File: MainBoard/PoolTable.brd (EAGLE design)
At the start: 457.2 x 166 mm, 75 parts, among them IC1 LM317MBSTT3, IC2 LM317MBSTT3, IC3 LM317MBSTT3, IC5 MIC2026-1YM, IC7 AP2331W-7, J1 USB_A_SMT_FEMALE, J2 USB_A_SMT_FEMALE, J4 SD_CARD_SOCKET, Q1 DMG1012T-7, Q2 DMG1012T-7, Q3 DMG1012T-7, U1 TMP102, U2 TMP102, U3 TMP102, U4 TMP102, U5 LAN9512-JZX, U6 FSUSB42UMX

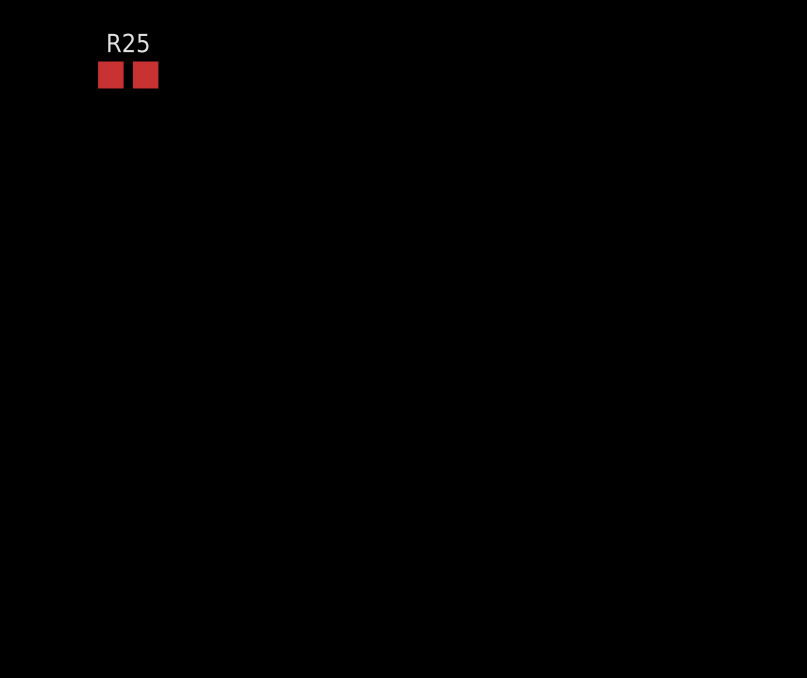
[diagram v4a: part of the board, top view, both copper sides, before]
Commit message: Implementing Cameras
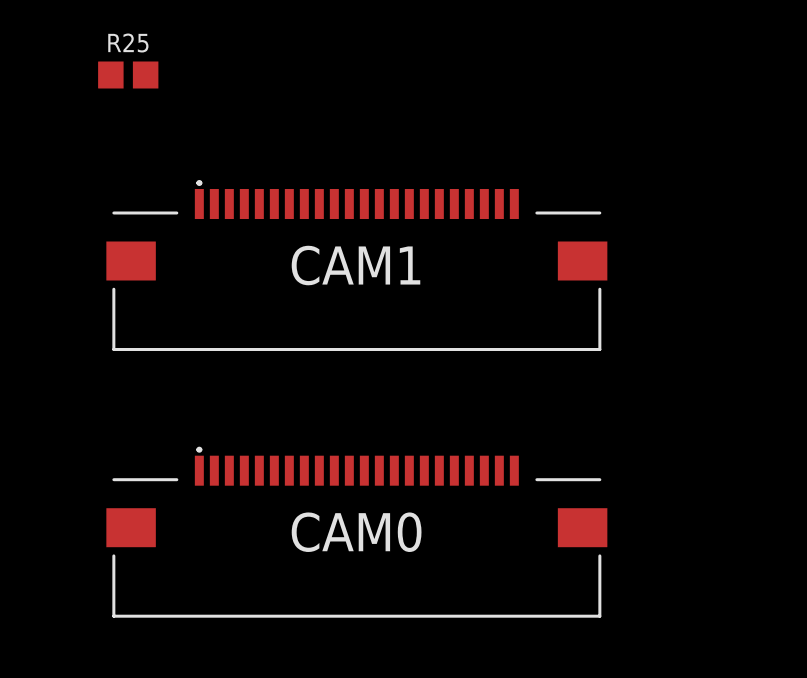
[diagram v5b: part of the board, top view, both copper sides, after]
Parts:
- added CAM0, CAM1: 54548-2271, SamacSys_Parts:545482271
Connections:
- new net CPU1_CAM0_C_N: CAM0.8
- new net CPU1_CAM0_C_P: CAM0.9
- new net CPU1_CAM0_D0_N: CAM0.2
- new net CPU1_CAM0_D0_P: CAM0.3
- new net CPU1_CAM0_D1_N: CAM0.5
- new net CPU1_CAM0_D1_P: CAM0.6
- new net CPU1_CAM0_IO_0: CAM0.17
- new net CPU1_CAM0_IO_1: CAM0.18
- new net CPU1_CAM1_C_N: CAM1.8, CPU1.149
- new net CPU1_CAM1_C_P: CAM1.9, CPU1.147
- new net CPU1_CAM1_D0_N: CAM1.2, CPU1.161
- new net CPU1_CAM1_D0_P: CAM1.3, CPU1.159
- new net CPU1_CAM1_D1_N: CAM1.5, CPU1.155
- new net CPU1_CAM1_D1_P: CAM1.6, CPU1.153
- new net CPU1_CAM1_D2_N: CAM1.11, CPU1.143
- new net CPU1_CAM1_D2_P: CAM1.12, CPU1.141
- new net CPU1_CAM1_D3_N: CAM1.14, CPU1.137
- new net CPU1_CAM1_D3_P: CAM1.15, CPU1.135
- new net CPU1_CAM1_IO_0: CAM1.17
- new net CPU1_CAM1_IO_1: CAM1.18
- new net CPU1_CD1_SCL: CAM0.20, CAM1.20
- new net CPU1_CD1_SDA: CAM0.21, CAM1.21
- net 3.3V: now also CAM0.22, CAM1.22
- net GND: now also CAM0.1, CAM0.10, CAM0.13, CAM0.16, CAM0.19, CAM0.23, CAM0.24, CAM0.4, CAM0.7, CAM1.1, CAM1.10, CAM1.13, CAM1.16, CAM1.19, CAM1.23, CAM1.24, CAM1.4, CAM1.7
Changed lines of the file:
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@@
 <attribute name="VALUE" x="-59.69" y="-436.372" size="0.6096" layer="27" font="vector" ratio="20" align="top-center"/>
+</element>
+<element name="CAM1" library="SamacSys_Parts" package="545482271" value="54548-2271" x="-52.07" y="-441.96" smashed="yes">
+<attribute name="DESCRIPTION" value="FFC &amp; FPC Connectors 0.5 FPC ZIF Hsg Assy ssy 22Ckt EmbsTp Pkg" x="-52.07" y="-441.96" size="1.778" layer="27" display="off"/>
+<attribute name="HEIGHT" value="1mm" x="-52.07" y="-441.96" size="1.778" layer="27" display="off"/>
+<attribute name="MANUFACTURER_NAME" value="Molex" x="-52.07" y="-441.96" size="1.778" layer="27" display="off"/>
+<attribute name="MANUFACTURER_PART_NUMBER" value="54548-2271" x="-52.07" y="-441.96" size="1.778" layer="27" display="off"/>
+<attribute name="MOUSER_PART_NUMBER" value="538-54548-2271" x="-52.07" y="-441.96" size="1.778" layer="27" display="off"/>
+<attribute name="NAME" x="-52.07" y="-441.96" size="1.27" layer="25" align="center"/>
+<attribute name="VALUE" x="-52.07" y="-441.96" size="1.27" layer="27" align="center"/>
+</element>
+<element name="CAM0" library="SamacSys_Parts" package="545482271" value="54548-2271" x="-52.07" y="-450.85" smashed="yes">
+<attribute name="DESCRIPTION" value="FFC &amp; FPC Connectors 0.5 FPC ZIF Hsg Assy ssy 22Ckt EmbsTp Pkg" x="-52.07" y="-450.85" size="1.778" layer="27" display="off"/>
+<attribute name="HEIGHT" value="1mm" x="-52.07" y="-450.85" size="1.778" layer="27" display="off"/>
+<attribute name="MANUFACTURER_NAME" value="Molex" x="-52.07" y="-450.85" size="1.778" layer="27" display="off"/>
+<attribute name="MANUFACTURER_PART_NUMBER" value="54548-2271" x="-52.07" y="-450.85" size="1.778" layer="27" display="off"/>
+<attribute name="MOUSER_PART_NUMBER" value="538-54548-2271" x="-52.07" y="-450.85" size="1.778" layer="27" display="off"/>
+<attribute name="NAME" x="-52.07" y="-450.85" size="1.27" layer="25" align="center"/>
+<attribute name="VALUE" x="-52.07" y="-450.85" size="1.27" layer="27" align="center"/>
 </element>
 </elements>
@@
 <contactref element="U$4" pad="2"/>
 <contactref element="U$5" pad="2"/>
+<contactref element="CAM1" pad="1"/>
+<contactref element="CAM1" pad="4"/>
+<contactref element="CAM1" pad="7"/>
+<contactref element="CAM1" pad="10"/>
+<contactref element="CAM1" pad="13"/>
+<contactref element="CAM1" pad="16"/>
+<contactref element="CAM1" pad="19"/>
+<contactref element="CAM1" pad="23"/>
+<contactref element="CAM1" pad="24"/>
+<contactref element="CAM0" pad="1"/>
+<contactref element="CAM0" pad="4"/>
+<contactref element="CAM0" pad="7"/>
+<contactref element="CAM0" pad="10"/>
+<contactref element="CAM0" pad="13"/>
+<contactref element="CAM0" pad="16"/>
+<contactref element="CAM0" pad="19"/>
+<contactref element="CAM0" pad="23"/>
+<contactref element="CAM0" pad="24"/>
+<wire x1="-55.82" y1="-448.8" x2="-57.32" y2="-448.8" width="0" layer="19" extent="1-1"/>
+<wire x1="-54.32" y1="-448.8" x2="-55.82" y2="-448.8" width="0" layer="19" extent="1-1"/>
+<wire x1="-52.82" y1="-448.8" x2="-54.32" y2="-448.8" width="0" layer="19" extent="1-1"/>
+<wire x1="-51.32" y1="-448.8" x2="-52.82" y2="-448.8" width="0" layer="19" extent="1-1"/>
+<wire x1="-49.82" y1="-448.8" x2="-51.32" y2="-448.8" width="0" layer="19" extent="1-1"/>
+<wire x1="-48.32" y1="-448.8" x2="-49.82" y2="-448.8" width="0" layer="19" extent="1-1"/>
+<wire x1="-59.595" y1="-450.7" x2="-57.32" y2="-448.8" width="0" layer="19" extent="1-1"/>
+<wire x1="-44.545" y1="-450.7" x2="-48.32" y2="-448.8" width="0" layer="19" extent="1-1"/>
+<wire x1="-59.595" y1="-441.81" x2="-57.32" y2="-448.8" width="0" layer="19" extent="1-1"/>
+<wire x1="-57.32" y1="-439.91" x2="-59.595" y2="-441.81" width="0" layer="19" extent="1-1"/>
+<wire x1="-55.82" y1="-439.91" x2="-57.32" y2="-439.91" width="0" layer="19" extent="1-1"/>
+<wire x1="-54.32" y1="-439.91" x2="-55.82" y2="-439.91" width="0" layer="19" extent="1-1"/>
+<wire x1="-52.82" y1="-439.91" x2="-54.32" y2="-439.91" width="0" layer="19" extent="1-1"/>
+<wire x1="-51.32" y1="-439.91" x2="-52.82" y2="-439.91" width="0" layer="19" extent="1-1"/>
+<wire x1="-49.82" y1="-439.91" x2="-51.32" y2="-439.91" width="0" layer="19" extent="1-1"/>
+<wire x1="-48.32" y1="-439.91" x2="-49.82" y2="-439.91" width="0" layer="19" extent="1-1"/>
+<wire x1="-44.545" y1="-441.81" x2="-48.32" y2="-439.91" width="0" layer="19" extent="1-1"/>
+<wire x1="-59.11" y1="-435.61" x2="-57.32" y2="-439.91" width="0" layer="19" extent="1-1"/>
 <wire x1="-59.11" y1="-431.8" x2="-59.11" y2="-435.61" width="0" layer="19" extent="1-1"/>
 <wire x1="-59.11" y1="-427.99" x2="-59.11" y2="-431.8" width="0" layer="19" extent="1-1"/>
@@
 <contactref element="C12" pad="1"/>
 <contactref element="SJ1" pad="2"/>
+<contactref element="CAM1" pad="22"/>
+<contactref element="CAM0" pad="22"/>
+<wire x1="-46.82" y1="-439.91" x2="-46.82" y2="-448.8" width="0" layer="19" extent="1-1"/>
+<wire x1="-58.928" y1="-416.56" x2="-46.82" y2="-439.91" width="0" layer="19" extent="1-1"/>
 <wire x1="-60.54" y1="-411.48" x2="-58.928" y2="-416.56" width="0" layer="19" extent="1-1"/>
 <wire x1="-60.69" y1="-395.7" x2="-60.54" y2="-411.48" width="0" layer="19" extent="1-1"/>
@@
 <contactref element="U5" pad="3"/>
 </signal>
+<signal name="CPU1_CAM1_D3_P" class="1">
+<contactref element="CPU1" pad="135"/>
+<contactref element="CAM1" pad="15"/>
+<wire x1="38.39" y1="55.6" x2="-50.32" y2="-439.91" width="0" layer="19" extent="1-1"/>
+</signal>
+<signal name="CPU1_CAM1_D3_N" class="1">
+<contactref element="CPU1" pad="137"/>
+<contactref element="CAM1" pad="14"/>
+<wire x1="38.39" y1="56.2" x2="-50.82" y2="-439.91" width="0" layer="19" extent="1-1"/>
+</signal>
+<signal name="CPU1_CAM1_D2_P" class="1">
+<contactref element="CPU1" pad="141"/>
+<contactref element="CAM1" pad="12"/>
+<wire x1="38.39" y1="57.4" x2="-51.82" y2="-439.91" width="0" layer="19" extent="1-1"/>
+</signal>
+<signal name="CPU1_CAM1_D2_N" class="1">
+<contactref element="CPU1" pad="143"/>
+<contactref element="CAM1" pad="11"/>
+<wire x1="38.39" y1="58" x2="-52.32" y2="-439.91" width="0" layer="19" extent="1-1"/>
+</signal>
+<signal name="CPU1_CAM1_C_P" class="1">
+<contactref element="CPU1" pad="147"/>
+<contactref element="CAM1" pad="9"/>
+<wire x1="38.39" y1="59.2" x2="-53.32" y2="-439.91" width="0" layer="19" extent="1-1"/>
+</signal>
+<signal name="CPU1_CAM1_C_N" class="1">
+<contactref element="CPU1" pad="149"/>
+<contactref element="CAM1" pad="8"/>
+<wire x1="38.39" y1="59.8" x2="-53.82" y2="-439.91" width="0" layer="19" extent="1-1"/>
+</signal>
+<signal name="CPU1_CAM1_D1_P" class="1">
+<contactref element="CPU1" pad="153"/>
+<contactref element="CAM1" pad="6"/>
+<wire x1="38.39" y1="61" x2="-54.82" y2="-439.91" width="0" layer="19" extent="1-1"/>
+</signal>
+<signal name="CPU1_CAM1_D1_N" class="1">
+<contactref element="CPU1" pad="155"/>
+<contactref element="CAM1" pad="5"/>
+<wire x1="38.39" y1="61.6" x2="-55.32" y2="-439.91" width="0" layer="19" extent="1-1"/>
+</signal>
+<signal name="CPU1_CAM1_D0_P" class="1">
+<contactref element="CPU1" pad="159"/>
+<contactref element="CAM1" pad="3"/>
+<wire x1="38.39" y1="62.8" x2="-56.32" y2="-439.91" width="0" layer="19" extent="1-1"/>
+</signal>
+<signal name="CPU1_CAM1_D0_N" class="1">
+<contactref element="CPU1" pad="161"/>
+<contactref element="CAM1" pad="2"/>
+<wire x1="38.39" y1="63.4" x2="-56.82" y2="-439.91" width="0" layer="19" extent="1-1"/>
+</signal>
+<signal name="CPU1_CAM1_IO_0">
+<contactref element="CAM1" pad="17"/>
+</signal>
+<signal name="CPU1_CAM1_IO_1">
+<contactref element="CAM1" pad="18"/>
+</signal>
+<signal name="CPU1_CD1_SCL">
+<contactref element="CAM1" pad="20"/>
+<contactref element="CAM0" pad="20"/>
+<wire x1="-47.82" y1="-439.91" x2="-47.82" y2="-448.8" width="0" layer="19" extent="1-1"/>
+</signal>
+<signal name="CPU1_CD1_SDA">
+<contactref element="CAM1" pad="21"/>
+<contactref element="CAM0" pad="21"/>
+<wire x1="-47.32" y1="-439.91" x2="-47.32" y2="-448.8" width="0" layer="19" extent="1-1"/>
+</signal>
+<signal name="CPU1_CAM0_D0_N">
+<contactref element="CAM0" pad="2"/>
+</signal>
+<signal name="CPU1_CAM0_D0_P">
+<contactref element="CAM0" pad="3"/>
+</signal>
+<signal name="CPU1_CAM0_D1_N">
+<contactref element="CAM0" pad="5"/>
+</signal>
+<signal name="CPU1_CAM0_D1_P">
+<contactref element="CAM0" pad="6"/>
+</signal>
+<signal name="CPU1_CAM0_C_N">
+<contactref element="CAM0" pad="8"/>
+</signal>
+<signal name="CPU1_CAM0_C_P">
+<contactref element="CAM0" pad="9"/>
+</signal>
+<signal name="CPU1_CAM0_IO_0">
+<contactref element="CAM0" pad="17"/>
+</signal>
+<signal name="CPU1_CAM0_IO_1">
+<contactref element="CAM0" pad="18"/>
+</signal>
 </signals>

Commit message: Syncing work
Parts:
- added SJ2, SJ3, SJ4, SJ5, SJ6, SJ7, SJ8, SJ9: (no value), jumper:SJ
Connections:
- removed net CPU1_CD1_SCL: CAM0.20, CAM1.20
- removed net CPU1_CD1_SDA: CAM0.21, CAM1.21
- new net CPU1_CAM0_IO0: SJ9.1
- new net CPU1_CAM0_IO1: SJ8.1
- new net CPU1_CAM0_SCL: SJ7.1
- new net CPU1_CAM0_SDA: SJ6.1
- new net CPU1_CAM1_IO0: SJ5.1
- new net CPU1_CAM1_IO1: SJ4.1
- new net CPU1_CAM1_SCL: SJ3.1
- new net CPU1_CAM1_SDA: SJ2.1
- net CPU1_CAM0_C_N: now also CPU1.144
- net CPU1_CAM0_C_P: now also CPU1.142
- net CPU1_CAM0_D0_N: now also CPU1.138
- net CPU1_CAM0_D0_P: now also CPU1.136
- net CPU1_CAM0_D1_N: now also CPU1.150
- net CPU1_CAM0_D1_P: now also CPU1.148
- net CPU1_GPIO28: now also SJ6.2
- net CPU1_GPIO29: now also SJ7.2
- net CPU1_GPIO30: now also SJ8.2
- net CPU1_GPIO31: now also SJ9.2
- net CPU1_SCL0: now also SJ3.2
- net CPU1_SCL1: now also SJ5.2
- net CPU1_SDA0: now also SJ2.2
- net CPU1_SDA1: now also SJ4.2
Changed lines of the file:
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@@
 <attribute name="VALUE" x="-52.07" y="-450.85" size="1.27" layer="27" align="center"/>
+</element>
+<element name="SJ2" library="jumper" library_urn="urn:adsk.eagle:library:252" package="SJ" package3d_urn="urn:adsk.eagle:package:15471/1" value="" x="-59.69" y="-458.47" smashed="yes">
+<attribute name="NAME" x="-61.341" y="-457.327" size="1.27" layer="25" ratio="10"/>
+<attribute name="VALUE" x="-59.2899" y="-458.47" size="0.02" layer="27"/>
+</element>
+<element name="SJ3" library="jumper" library_urn="urn:adsk.eagle:library:252" package="SJ" package3d_urn="urn:adsk.eagle:package:15471/1" value="" x="-59.69" y="-463.55" smashed="yes">
+<attribute name="NAME" x="-61.341" y="-462.407" size="1.27" layer="25" ratio="10"/>
+<attribute name="VALUE" x="-59.2899" y="-463.55" size="0.02" layer="27"/>
+</element>
+<element name="SJ4" library="jumper" library_urn="urn:adsk.eagle:library:252" package="SJ" package3d_urn="urn:adsk.eagle:package:15471/1" value="" x="-59.69" y="-468.63" smashed="yes">
+<attribute name="NAME" x="-61.341" y="-467.487" size="1.27" layer="25" ratio="10"/>
+<attribute name="VALUE" x="-59.2899" y="-468.63" size="0.02" layer="27"/>
+</element>
+<element name="SJ5" library="jumper" library_urn="urn:adsk.eagle:library:252" package="SJ" package3d_urn="urn:adsk.eagle:package:15471/1" value="" x="-59.69" y="-473.71" smashed="yes">
+<attribute name="NAME" x="-61.341" y="-472.567" size="1.27" layer="25" ratio="10"/>
+<attribute name="VALUE" x="-59.2899" y="-473.71" size="0.02" layer="27"/>
+</element>
+<element name="SJ6" library="jumper" library_urn="urn:adsk.eagle:library:252" package="SJ" package3d_urn="urn:adsk.eagle:package:15471/1" value="" x="-59.69" y="-478.79" smashed="yes">
+<attribute name="NAME" x="-61.341" y="-477.647" size="1.27" layer="25" ratio="10"/>
+<attribute name="VALUE" x="-59.2899" y="-478.79" size="0.02" layer="27"/>
+</element>
+<element name="SJ7" library="jumper" library_urn="urn:adsk.eagle:library:252" package="SJ" package3d_urn="urn:adsk.eagle:package:15471/1" value="" x="-59.69" y="-483.87" smashed="yes">
+<attribute name="NAME" x="-61.341" y="-482.727" size="1.27" layer="25" ratio="10"/>
+<attribute name="VALUE" x="-59.2899" y="-483.87" size="0.02" layer="27"/>
+</element>
+<element name="SJ8" library="jumper" library_urn="urn:adsk.eagle:library:252" package="SJ" package3d_urn="urn:adsk.eagle:package:15471/1" value="" x="-59.69" y="-488.95" smashed="yes">
+<attribute name="NAME" x="-61.341" y="-487.807" size="1.27" layer="25" ratio="10"/>
+<attribute name="VALUE" x="-59.2899" y="-488.95" size="0.02" layer="27"/>
+</element>
+<element name="SJ9" library="jumper" library_urn="urn:adsk.eagle:library:252" package="SJ" package3d_urn="urn:adsk.eagle:package:15471/1" value="" x="-59.69" y="-494.03" smashed="yes">
+<attribute name="NAME" x="-61.341" y="-492.887" size="1.27" layer="25" ratio="10"/>
+<attribute name="VALUE" x="-59.2899" y="-494.03" size="0.02" layer="27"/>
 </element>
 </elements>
@@
 <contactref element="U$3" pad="SDA"/>
 <contactref element="U$2" pad="SDA"/>
+<contactref element="SJ2" pad="2"/>
 <wire x1="19.05" y1="-212.09" x2="19.05" y2="-242.57" width="0" layer="19" extent="1-1"/>
 <wire x1="19.05" y1="-181.61" x2="19.05" y2="-212.09" width="0" layer="19" extent="1-1"/>
@@
 <wire x1="-1.763584375" y1="-121.42203125" x2="-5.573584375" y2="-121.42203125" width="0" layer="19" extent="1-1"/>
 <wire x1="38.39" y1="12.4" x2="-1.763584375" y2="-121.42203125" width="0" layer="19" extent="1-1"/>
+<wire x1="-58.928" y1="-458.47" x2="19.05" y2="-242.57" width="0" layer="19" extent="1-1"/>
 </signal>
 <signal name="CPU1_SCL0">
@@
 <contactref element="U$3" pad="SCL"/>
 <contactref element="U$2" pad="SCL"/>
+<contactref element="SJ3" pad="2"/>
 <wire x1="19.05" y1="-214.63" x2="19.05" y2="-245.11" width="0" layer="19" extent="1-1"/>
 <wire x1="19.05" y1="-184.15" x2="19.05" y2="-214.63" width="0" layer="19" extent="1-1"/>
@@
 <wire x1="-3.34" y1="-121.42203125" x2="-7.15" y2="-121.42203125" width="0" layer="19" extent="1-1"/>
 <wire x1="38.39" y1="13" x2="-3.34" y2="-121.42203125" width="0" layer="19" extent="1-1"/>
+<wire x1="-58.928" y1="-463.55" x2="19.05" y2="-245.11" width="0" layer="19" extent="1-1"/>
 </signal>
 <signal name="CPU1_SDA1">
 <contactref element="CPU1" pad="9"/>
 <contactref element="R11" pad="1"/>
+<contactref element="SJ4" pad="2"/>
 <wire x1="38.39" y1="14.2" x2="-11.01" y2="-175.26" width="0" layer="19" extent="1-1"/>
+<wire x1="-58.928" y1="-468.63" x2="-11.01" y2="-175.26" width="0" layer="19" extent="1-1"/>
 </signal>
 <signal name="CPU1_SCL1">
 <contactref element="CPU1" pad="11"/>
 <contactref element="R10" pad="1"/>
+<contactref element="SJ5" pad="2"/>
 <wire x1="38.39" y1="14.8" x2="-11.01" y2="-171.45" width="0" layer="19" extent="1-1"/>
+<wire x1="-58.928" y1="-473.71" x2="-11.01" y2="-171.45" width="0" layer="19" extent="1-1"/>
 </signal>
 <signal name="CPU1_GPIO4">
@@
 <contactref element="CPU1" pad="28"/>
 <contactref element="R22" pad="1"/>
+<contactref element="SJ6" pad="2"/>
+<wire x1="-58.928" y1="-478.79" x2="-60.27" y2="-424.18" width="0" layer="19" extent="1-1"/>
 <wire x1="30.19" y1="19.9" x2="-60.27" y2="-424.18" width="0" layer="19" extent="1-1"/>
 </signal>
@@
 <contactref element="CPU1" pad="30"/>
 <contactref element="R23" pad="1"/>
+<contactref element="SJ7" pad="2"/>
+<wire x1="-58.928" y1="-483.87" x2="-60.27" y2="-427.99" width="0" layer="19" extent="1-1"/>
 <wire x1="30.19" y1="20.5" x2="-60.27" y2="-427.99" width="0" layer="19" extent="1-1"/>
 </signal>
 <signal name="CPU1_GPIO30">
 <contactref element="CPU1" pad="34"/>
+<contactref element="SJ8" pad="2"/>
+<wire x1="-58.928" y1="-488.95" x2="30.19" y2="21.7" width="0" layer="19" extent="1-1"/>
 </signal>
 <signal name="CPU1_GPIO31">
 <contactref element="CPU1" pad="36"/>
+<contactref element="SJ9" pad="2"/>
+<wire x1="-58.928" y1="-494.03" x2="30.19" y2="22.3" width="0" layer="19" extent="1-1"/>
 </signal>
 <signal name="CPU1_GPIO32">
@@
 <contactref element="CAM1" pad="18"/>
 </signal>
-<signal name="CPU1_CD1_SCL">
-<contactref element="CAM1" pad="20"/>
-<contactref element="CAM0" pad="20"/>
-<wire x1="-47.82" y1="-439.91" x2="-47.82" y2="-448.8" width="0" layer="19" extent="1-1"/>
-</signal>
-<signal name="CPU1_CD1_SDA">
-<contactref element="CAM1" pad="21"/>
-<contactref element="CAM0" pad="21"/>
-<wire x1="-47.32" y1="-439.91" x2="-47.32" y2="-448.8" width="0" layer="19" extent="1-1"/>
-</signal>
-<signal name="CPU1_CAM0_D0_N">
+<signal name="CPU1_CAM0_D0_N" class="1">
 <contactref element="CAM0" pad="2"/>
-</signal>
-<signal name="CPU1_CAM0_D0_P">
+<contactref element="CPU1" pad="138"/>
+<wire x1="30.19" y1="56.5" x2="-56.82" y2="-448.8" width="0" layer="19" extent="1-1"/>
+</signal>
+<signal name="CPU1_CAM0_D0_P" class="1">
 <contactref element="CAM0" pad="3"/>
-</signal>
-<signal name="CPU1_CAM0_D1_N">
+<contactref element="CPU1" pad="136"/>
+<wire x1="30.19" y1="55.9" x2="-56.32" y2="-448.8" width="0" layer="19" extent="1-1"/>
+</signal>
+<signal name="CPU1_CAM0_D1_N" class="1">
 <contactref element="CAM0" pad="5"/>
-</signal>
-<signal name="CPU1_CAM0_D1_P">
+<contactref element="CPU1" pad="150"/>
+<wire x1="30.19" y1="60.1" x2="-55.32" y2="-448.8" width="0" layer="19" extent="1-1"/>
+</signal>
+<signal name="CPU1_CAM0_D1_P" class="1">
 <contactref element="CAM0" pad="6"/>
-</signal>
-<signal name="CPU1_CAM0_C_N">
+<contactref element="CPU1" pad="148"/>
+<wire x1="30.19" y1="59.5" x2="-54.82" y2="-448.8" width="0" layer="19" extent="1-1"/>
+</signal>
+<signal name="CPU1_CAM0_C_N" class="1">
 <contactref element="CAM0" pad="8"/>
-</signal>
-<signal name="CPU1_CAM0_C_P">
+<contactref element="CPU1" pad="144"/>
+<wire x1="30.19" y1="58.3" x2="-53.82" y2="-448.8" width="0" layer="19" extent="1-1"/>
+</signal>
+<signal name="CPU1_CAM0_C_P" class="1">
 <contactref element="CAM0" pad="9"/>
+<contactref element="CPU1" pad="142"/>
+<wire x1="30.19" y1="57.7" x2="-53.32" y2="-448.8" width="0" layer="19" extent="1-1"/>
 </signal>
 <signal name="CPU1_CAM0_IO_0">
@@
 <contactref element="CAM0" pad="18"/>
 </signal>
+<signal name="CPU1_CAM1_SDA">
+<contactref element="SJ2" pad="1"/>
+</signal>
+<signal name="CPU1_CAM1_SCL">
+<contactref element="SJ3" pad="1"/>
+</signal>
+<signal name="CPU1_CAM1_IO0">
+<contactref element="SJ5" pad="1"/>
+</signal>
+<signal name="CPU1_CAM0_SDA">
+<contactref element="SJ6" pad="1"/>
+</signal>
+<signal name="CPU1_CAM0_SCL">
+<contactref element="SJ7" pad="1"/>
+</signal>
+<signal name="CPU1_CAM0_IO1">
+<contactref element="SJ8" pad="1"/>
+</signal>
+<signal name="CPU1_CAM0_IO0">
+<contactref element="SJ9" pad="1"/>
+</signal>
+<signal name="CPU1_CAM1_IO1">
+<contactref element="SJ4" pad="1"/>
+</signal>
 </signals>
